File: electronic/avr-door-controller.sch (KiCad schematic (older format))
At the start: 74 parts, among them CON1 24V, J1 DOOR1, J2 DOOR2, K1 RELAY, K2 RELAY, P1 Digital, P10 DOOR2 BTN, P2 Analog, P3 DOOR1 BTN, P6 USB_A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

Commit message: electronic: schematics: Set the footprints of the new components
Signed-off-by: Alban Bedel <albeu@free.fr>
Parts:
- D4, D5: value D -> 1N4148; footprint (none) -> Diodes_ThroughHole:Diode_DO-35_SOD27_Horizontal_RM10
- K1, K2: footprint (none) -> Modules:JRC-21F
- U3: footprint (none) -> Modules:MT3608
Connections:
- wire segments 209 -> 189

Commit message: electronic: schematics: Use DO35 footprint for all the zener diodes
It turned out to be easy to find DO35 zener dione with the proper
rating. We used that on the rev 0 board but the holes are a bit too
large which is annoying when soldering, so move to DO35 footprints.

Signed-off-by: Alban Bedel <albeu@free.fr>
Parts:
- D12, D13, D14, D2, D3, D6, D7, D8, D9: footprint Diodes_ThroughHole:Diode_DO-41_SOD81_Horizontal_RM10 -> Diodes_ThroughHole:Diode_DO-35_SOD27_Horizontal_RM10
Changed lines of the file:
@@
 F 0 "D6" H 3400 2900 50  0000 C CNN
 F 1 "5.1V" H 3400 2700 50  0000 C CNN
-F 2 "Diodes_ThroughHole:Diode_DO-41_SOD81_Horizontal_RM10" H 3400 2800 50  0001 C CNN
+F 2 "Diodes_ThroughHole:Diode_DO-35_SOD27_Horizontal_RM10" H 3400 2800 50  0001 C CNN
 F 3 "" H 3400 2800 50  0000 C CNN
 F 4 "500m" H 3400 2800 60  0001 C CNN "Pd"
@@
 F 0 "D8" H 3400 3700 50  0000 C CNN
 F 1 "5.1V" H 3400 3500 50  0000 C CNN
-F 2 "Diodes_ThroughHole:Diode_DO-41_SOD81_Horizontal_RM10" H 3400 3600 50  0001 C CNN
+F 2 "Diodes_ThroughHole:Diode_DO-35_SOD27_Horizontal_RM10" H 3400 3600 50  0001 C CNN
 F 3 "" H 3400 3600 50  0000 C CNN
 F 4 "500m" H 3400 3600 60  0001 C CNN "Pd"
@@
 F 0 "D7" H 3400 3300 50  0000 C CNN
 F 1 "5.1V" H 3400 3100 50  0000 C CNN
-F 2 "Diodes_ThroughHole:Diode_DO-41_SOD81_Horizontal_RM10" H 3400 3200 50  0001 C CNN
+F 2 "Diodes_ThroughHole:Diode_DO-35_SOD27_Horizontal_RM10" H 3400 3200 50  0001 C CNN
 F 3 "" H 3400 3200 50  0000 C CNN
 F 4 "500m" H 3400 3200 60  0001 C CNN "Pd"
@@
 F 0 "D3" H 1650 2200 50  0000 C CNN
 F 1 "5.1V" H 1650 2000 50  0000 C CNN
-F 2 "Diodes_ThroughHole:Diode_DO-41_SOD81_Horizontal_RM10" H 1650 2100 50  0001 C CNN
+F 2 "Diodes_ThroughHole:Diode_DO-35_SOD27_Horizontal_RM10" H 1650 2100 50  0001 C CNN
 F 3 "" H 1650 2100 50  0000 C CNN
 F 4 "500m" H 1650 2100 60  0001 C CNN "Pd"
@@
 F 0 "D12" H 8400 2900 50  0000 C CNN
 F 1 "5.1V" H 8400 2700 50  0000 C CNN
-F 2 "Diodes_ThroughHole:Diode_DO-41_SOD81_Horizontal_RM10" H 8400 2800 50  0001 C CNN
+F 2 "Diodes_ThroughHole:Diode_DO-35_SOD27_Horizontal_RM10" H 8400 2800 50  0001 C CNN
 F 3 "" H 8400 2800 50  0000 C CNN
 F 4 "500m" H 8400 2800 60  0001 C CNN "Pd"
@@
 F 0 "D14" H 8400 3700 50  0000 C CNN
 F 1 "5.1V" H 8400 3500 50  0000 C CNN
-F 2 "Diodes_ThroughHole:Diode_DO-41_SOD81_Horizontal_RM10" H 8400 3600 50  0001 C CNN
+F 2 "Diodes_ThroughHole:Diode_DO-35_SOD27_Horizontal_RM10" H 8400 3600 50  0001 C CNN
 F 3 "" H 8400 3600 50  0000 C CNN
 F 4 "500m" H 8400 3600 60  0001 C CNN "Pd"
@@
 F 0 "D13" H 8400 3300 50  0000 C CNN
 F 1 "5.1V" H 8400 3100 50  0000 C CNN
-F 2 "Diodes_ThroughHole:Diode_DO-41_SOD81_Horizontal_RM10" H 8400 3200 50  0001 C CNN
+F 2 "Diodes_ThroughHole:Diode_DO-35_SOD27_Horizontal_RM10" H 8400 3200 50  0001 C CNN
 F 3 "" H 8400 3200 50  0000 C CNN
 F 4 "500m" H 8400 3200 60  0001 C CNN "Pd"
@@
 F 0 "D9" H 10150 2200 50  0000 C CNN
 F 1 "5.1V" H 10150 2000 50  0000 C CNN
-F 2 "Diodes_ThroughHole:Diode_DO-41_SOD81_Horizontal_RM10" H 10150 2100 50  0001 C CNN
+F 2 "Diodes_ThroughHole:Diode_DO-35_SOD27_Horizontal_RM10" H 10150 2100 50  0001 C CNN
 F 3 "" H 10150 2100 50  0000 C CNN
 F 4 "500m" H 10150 2100 60  0001 C CNN "Pd"
@@
 F 0 "D2" H 3050 7050 50  0000 C CNN
 F 1 "5.1V" H 3050 6850 50  0000 C CNN
-F 2 "Diodes_ThroughHole:Diode_DO-41_SOD81_Horizontal_RM10" H 3050 6950 50  0001 C CNN
+F 2 "Diodes_ThroughHole:Diode_DO-35_SOD27_Horizontal_RM10" H 3050 6950 50  0001 C CNN
 F 3 "" H 3050 6950 50  0000 C CNN
 	1    3050 6950

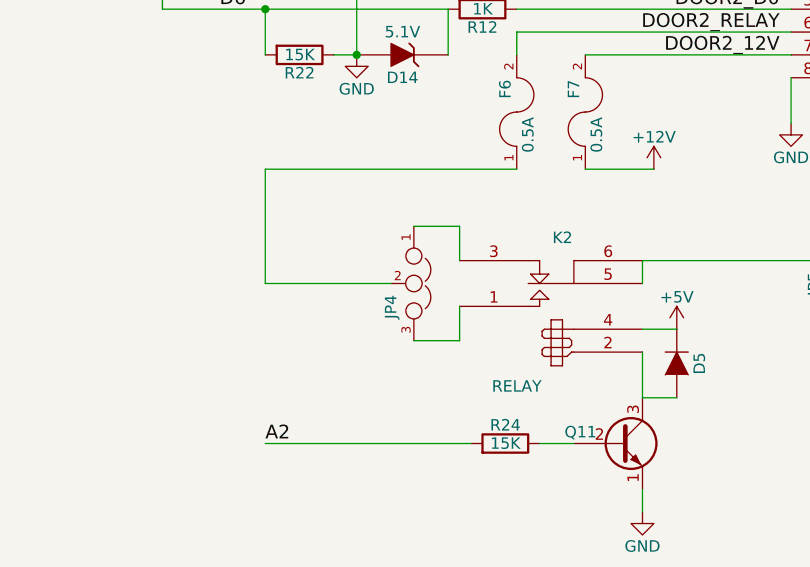
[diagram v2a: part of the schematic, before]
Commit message: electronic: schematics: Update the jumper labels for the PCB
To avoid using custom labels on the PCB just set the one we needs in
the schematics. While at it also flip JP4 to match the pinout of JP3,
that way they have the same orientation on the PCB.

Signed-off-by: Alban Bedel <alban.bedel@avionic-design.de>
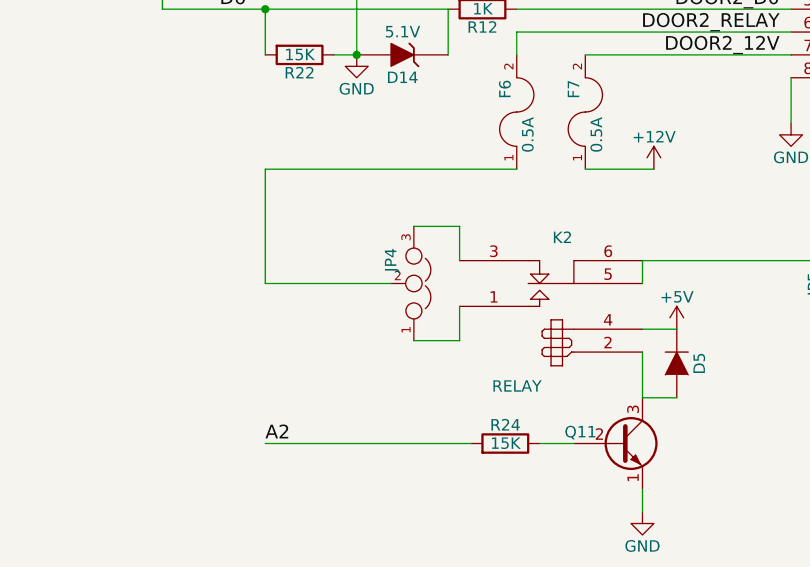
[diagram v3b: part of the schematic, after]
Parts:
- JP1: value DR1 VCC -> 12V|24V
- JP2: value DR1 LVL -> VCC|GND
- JP3: value DR1 NO/NC -> NC | NO
- JP4: value DR2 NO/NC -> NC | NO
- JP5: value DR2 LVL -> VCC|GND
- JP6: value DR2 VCC -> 12V|24V
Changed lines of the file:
@@
 P 1500 4500
 F 0 "JP2" H 1550 4400 50  0000 L CNN
-F 1 "DR1 LVL" H 1500 4600 50  0001 C BNN
+F 1 "VCC|GND" H 1500 4600 50  0001 C BNN
 F 2 "Connect:PINHEAD1-3" H 1500 4500 50  0001 C CNN
 F 3 "" H 1500 4500 50  0000 C CNN
@@
 P 1150 4500
 F 0 "JP1" H 1200 4400 50  0000 L CNN
-F 1 "DR1 VCC" H 1150 4600 50  0001 C BNN
+F 1 "12V|24V" H 1150 4600 50  0001 C BNN
 F 2 "Connect:PINHEAD1-3" H 1150 4500 50  0001 C CNN
 F 3 "" H 1150 4500 50  0000 C CNN
@@
 P 3350 4600
 F 0 "JP3" H 3400 4500 50  0000 L CNN
-F 1 "DR1 NO/NC" H 3350 4700 50  0001 C BNN
+F 1 "NC | NO" H 3350 4700 50  0001 C BNN
 F 2 "Connect:PINHEAD1-3" H 3350 4600 50  0001 C CNN
 F 3 "" H 3350 4600 50  0000 C CNN
@@
 P 10300 4500
 F 0 "JP5" H 10350 4400 50  0000 L CNN
-F 1 "DR2 LVL" H 10300 4600 50  0001 C BNN
+F 1 "VCC|GND" H 10300 4600 50  0001 C BNN
 F 2 "Connect:PINHEAD1-3" H 10300 4500 50  0001 C CNN
 F 3 "" H 10300 4500 50  0000 C CNN
@@
 P 10650 4500
 F 0 "JP6" H 10700 4400 50  0000 L CNN
-F 1 "DR2 VCC" H 10650 4600 50  0001 C BNN
+F 1 "12V|24V" H 10650 4600 50  0001 C BNN
 F 2 "Connect:PINHEAD1-3" H 10650 4500 50  0001 C CNN
 F 3 "" H 10650 4500 50  0000 C CNN
@@
 P 8450 4600
 F 0 "JP4" H 8500 4500 50  0000 L CNN
-F 1 "DR2 NO/NC" H 8450 4700 50  0001 C BNN
+F 1 "NC | NO" H 8450 4700 50  0001 C BNN
 F 2 "Connect:PINHEAD1-3" H 8450 4600 50  0001 C CNN
 F 3 "" H 8450 4600 50  0000 C CNN
 	1    8450 4600
-	0    1    1    0
+	0    1    -1   0
 $EndComp
 Text Label 7800 5300 0    60   ~ 0

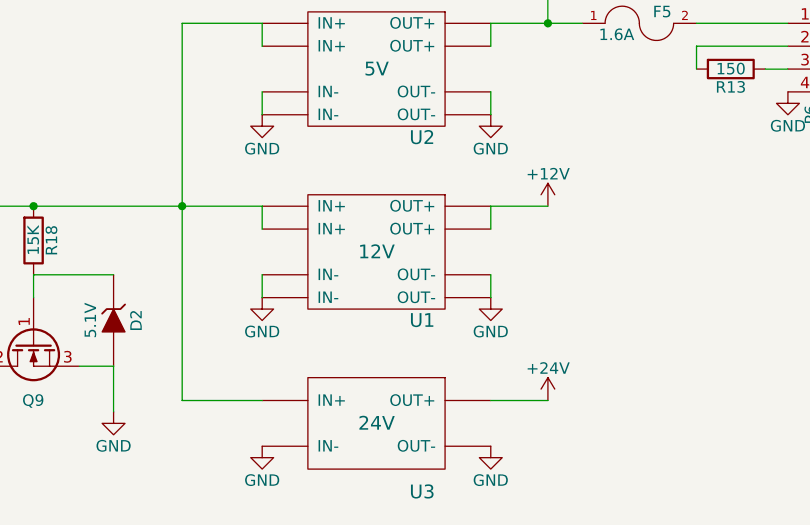
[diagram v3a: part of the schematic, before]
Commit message: electronic: schematics: Add a jumper to select the input voltage
To support both the step-up and step-down config we need to connect
either the +12V or the +24V with the input voltage. This would mean
adding a ratline on the PCB, which is not very nice. Instead we add a
jumper footprint where one can easily solder a wire, along with the
label it make it clearly visible which input voltage the board expect.

Signed-off-by: Alban Bedel <alban.bedel@avionic-design.de>
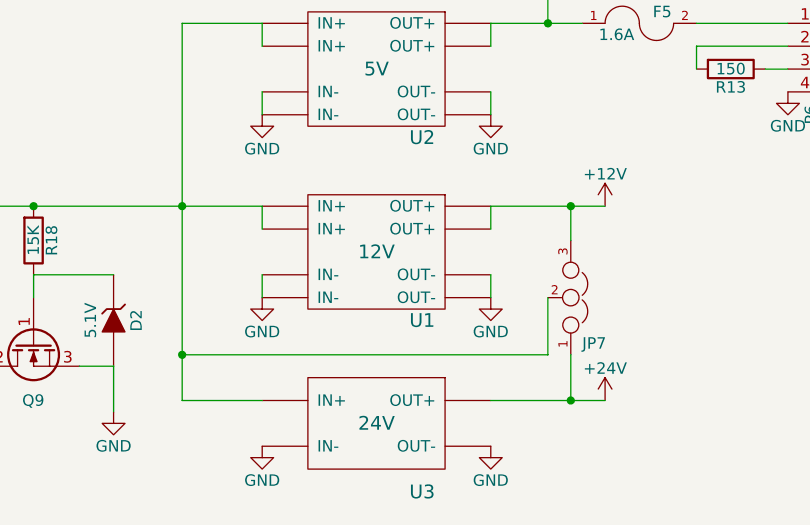
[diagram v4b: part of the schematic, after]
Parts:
- added JP7: 12V|24V, Connect:PINHEAD1-3, symbol JUMPER3
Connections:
- wire segments 189 -> 193
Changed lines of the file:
@@
 L +12V #PWR019
 U 1 1 58EFEBD6
-P 4950 6450
-F 0 "#PWR019" H 4950 6300 50  0001 C CNN
-F 1 "+12V" H 4950 6590 50  0000 C CNN
-F 2 "" H 4950 6450 50  0000 C CNN
-F 3 "" H 4950 6450 50  0000 C CNN
-	1    4950 6450
+P 5200 6450
+F 0 "#PWR019" H 5200 6300 50  0001 C CNN
+F 1 "+12V" H 5200 6590 50  0000 C CNN
+F 2 "" H 5200 6450 50  0000 C CNN
+F 3 "" H 5200 6450 50  0000 C CNN
+	1    5200 6450
 	1    0    0    -1
 $EndComp
@@
 	2200 6450 3700 6450
 Wire Wire Line
-	4700 6450 4950 6450
+	4700 6450 5200 6450
 Wire Wire Line
 	4700 5650 5100 5650
@@
 L +24V #PWR036
 U 1 1 59BF6F6A
-P 4950 7300
-F 0 "#PWR036" H 4950 7150 50  0001 C CNN
-F 1 "+24V" H 4950 7440 50  0000 C CNN
-F 2 "" H 4950 7300 50  0000 C CNN
-F 3 "" H 4950 7300 50  0000 C CNN
-	1    4950 7300
-	1    0    0    -1
-$EndComp
-Wire Wire Line
-	4700 7300 4950 7300
+P 5200 7300
+F 0 "#PWR036" H 5200 7150 50  0001 C CNN
+F 1 "+24V" H 5200 7440 50  0000 C CNN
+F 2 "" H 5200 7300 50  0000 C CNN
+F 3 "" H 5200 7300 50  0000 C CNN
+	1    5200 7300
+	1    0    0    -1
+$EndComp
+Wire Wire Line
+	4700 7300 5200 7300
 $Comp
 L GND #PWR037
@@
 	3350 7300 3700 7300
 Connection ~ 3350 6450
+$Comp
+L JUMPER3 JP7
+U 1 1 5A04918D
+P 5050 6850
+F 0 "JP7" V 4850 6900 50  0000 L CNN
+F 1 "12V|24V" H 5050 6950 50  0001 C BNN
+F 2 "Connect:PINHEAD1-3" H 5050 6850 50  0001 C CNN
+F 3 "" H 5050 6850 50  0000 C CNN
+	1    5050 6850
+	0    1    -1   0
+$EndComp
+Wire Wire Line
+	5050 7300 5050 7100
+Connection ~ 5050 7300
+Wire Wire Line
+	5050 6450 5050 6600
+Connection ~ 5050 6450
+Wire Wire Line
+	4950 6850 4950 7100
+Wire Wire Line
+	4950 7100 3350 7100
+Connection ~ 3350 7100
 $EndSCHEMATC
